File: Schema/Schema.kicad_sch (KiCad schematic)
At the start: 2 parts, among them U1 NodeMCU1.0(ESP-12E)

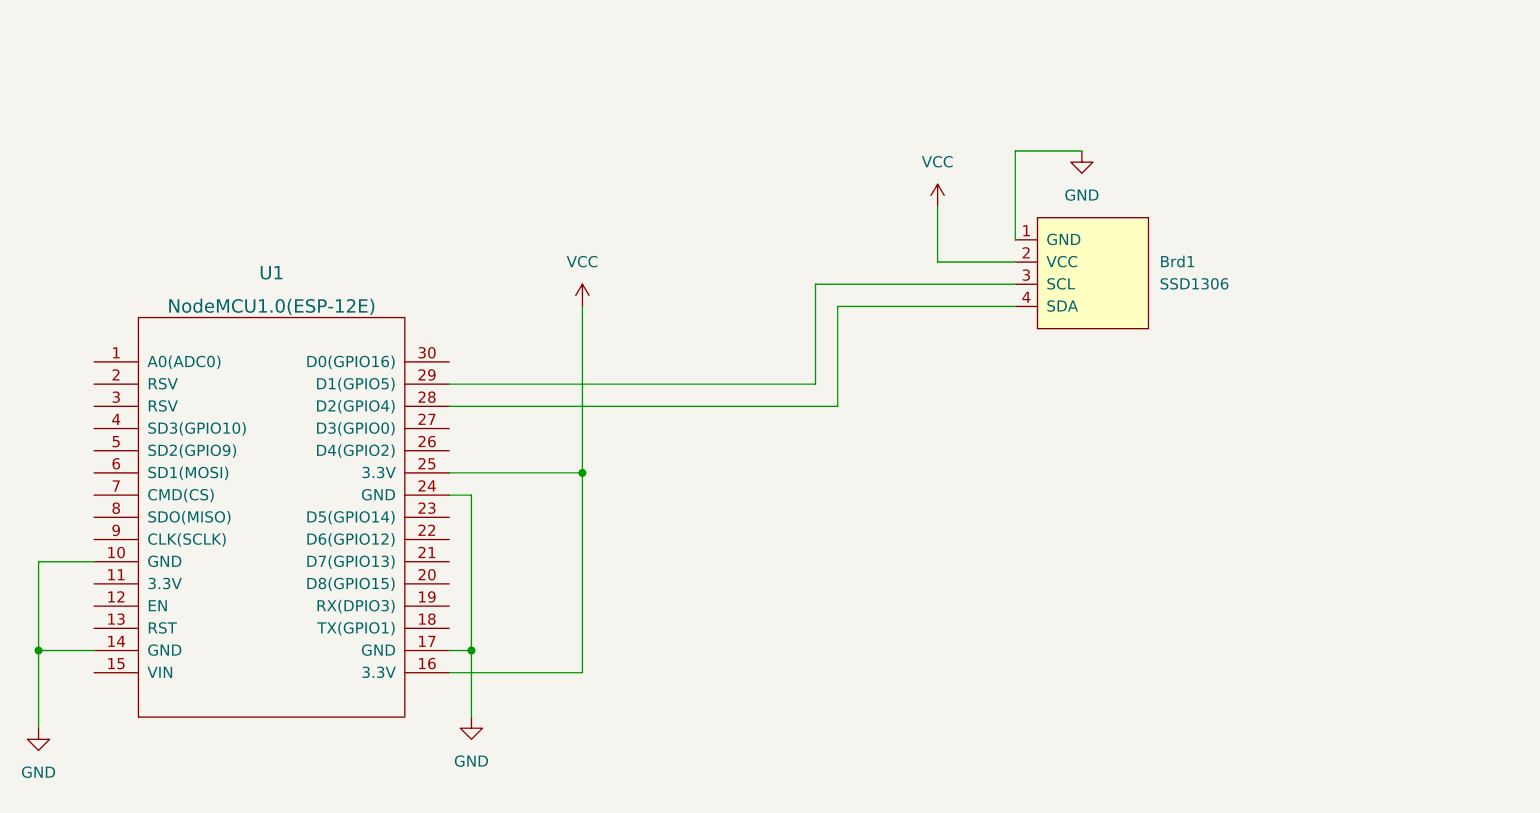
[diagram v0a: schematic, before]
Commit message: Add DHT22
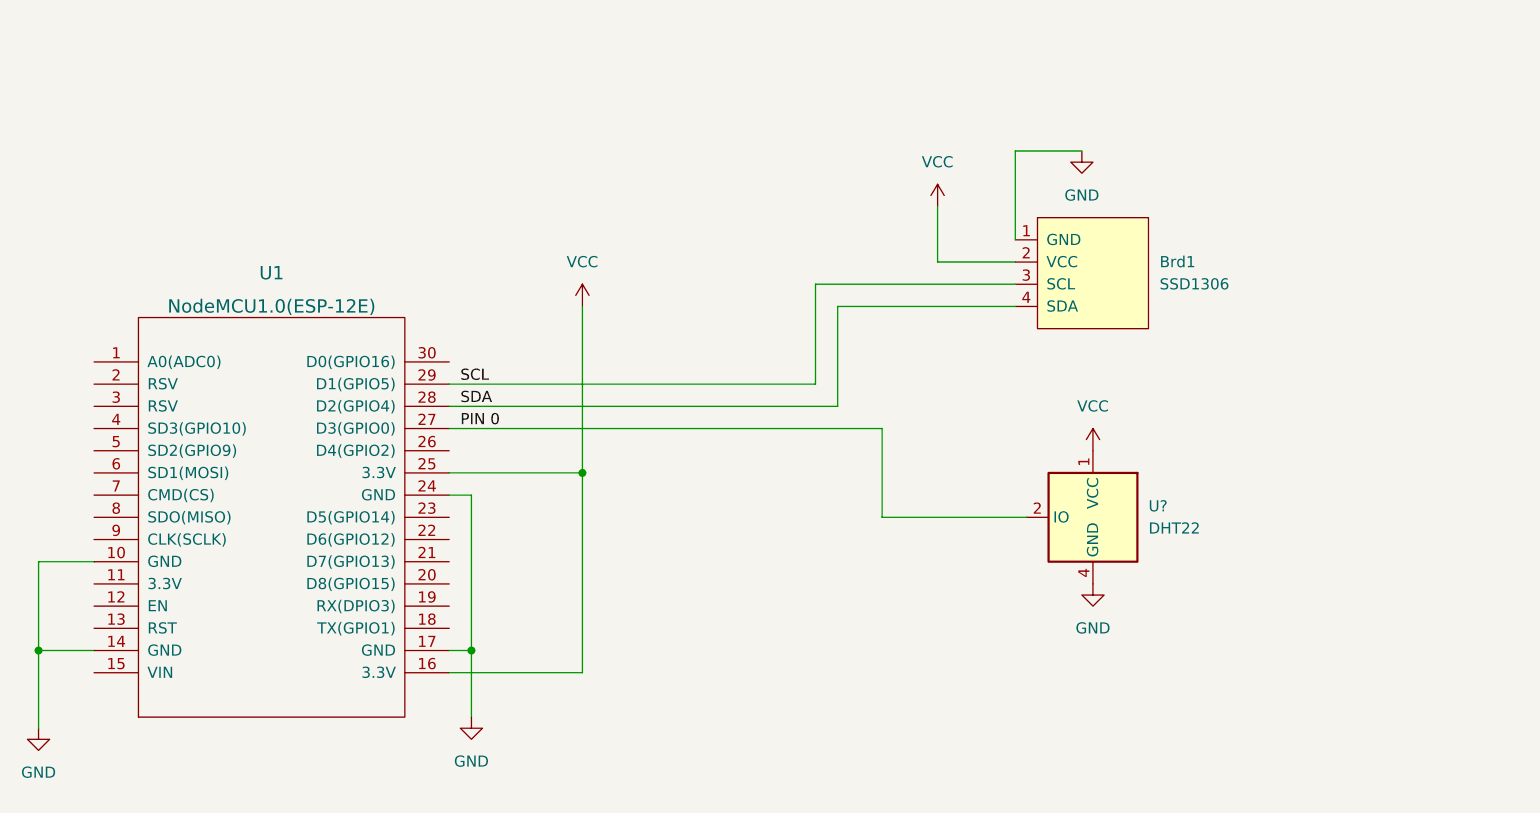
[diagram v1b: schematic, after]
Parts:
- added U?: DHT22, Sensor:Aosong_DHT11_5.5x12.0_P2.54mm, symbol Sensor:DHT11
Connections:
- net GND: now also U?.4 (GND)
- net VCC: now also U?.1 (VCC)
- net SCL: now reaches Brd1.3 (SCL), U1.29 (D1(GPIO5))
- net SDA: now reaches Brd1.4 (SDA), U1.28 (D2(GPIO4))
- net PIN 0: now reaches U1.27 (D3(GPIO0))
- net PIN 0: now also U?.2 (IO)
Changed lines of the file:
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@@
   (junction (at 147.32 90.17) (diameter 0) (color 0 0 0 0)
   )
+  (wire (pts (xy 194.31 64.77) (xy 144.78 64.77))
+    (stroke (width 0) (type default) (color 0 0 0 0))
+  )
+  (wire (pts (xy 194.31 74.93) (xy 194.31 64.77))
+    (stroke (width 0) (type default) (color 0 0 0 0))
+  )
   (wire (pts (xy 147.32 90.17) (xy 147.32 97.79))
     (stroke (width 0) (type default) (color 0 0 0 0))
@@
     (stroke (width 0) (type default) (color 0 0 0 0))
   )
+  (wire (pts (xy 210.82 74.93) (xy 194.31 74.93))
+    (stroke (width 0) (type default) (color 0 0 0 0))
+  )
   (wire (pts (xy 160.02 92.71) (xy 160.02 69.85))
     (stroke (width 0) (type default) (color 0 0 0 0))
@@
   (wire (pts (xy 200.66 39.37) (xy 200.66 45.72))
     (stroke (width 0) (type default) (color 0 0 0 0))
+  )
+  (label "PIN 0" (at 146.05 64.77 0)
+    (effects (font (size 1.27 1.27)) (justify left bottom))
+  )
+  (label "SCL" (at 146.05 59.69 0)
+    (effects (font (size 1.27 1.27)) (justify left bottom))
+  )
+  (label "SDA" (at 146.05 62.23 0)
+    (effects (font (size 1.27 1.27)) (justify left bottom))
   )
   (symbol (lib_id "power:VCC") (at 200.66 39.37 0) (unit 1)
@@
     )
     (property "Datasheet" "" (id 3) (at 147.32 97.79 0)
+      (effects (font (size 1.27 1.27)) hide)
+    )
+    (pin "1")
+  )
+  (symbol (lib_id "power:VCC") (at 218.44 67.31 0) (unit 1)
+    (in_bom yes) (on_board yes) (fields_autoplaced)
+    (property "Reference" "#PWR?" (id 0) (at 218.44 71.12 0)
+      (effects (font (size 1.27 1.27)) hide)
+    )
+    (property "Value" "VCC" (id 1) (at 218.44 62.23 0))
+    (property "Footprint" "" (id 2) (at 218.44 67.31 0)
+      (effects (font (size 1.27 1.27)) hide)
+    )
+    (property "Datasheet" "" (id 3) (at 218.44 67.31 0)
       (effects (font (size 1.27 1.27)) hide)
     )
@@
     )
     (property "Datasheet" "" (id 3) (at 160.02 50.8 0)
+      (effects (font (size 1.27 1.27)) hide)
+    )
+    (pin "1")
+  )
+  (symbol (lib_id "power:GND") (at 218.44 82.55 0) (unit 1)
+    (in_bom yes) (on_board yes) (fields_autoplaced)
+    (property "Reference" "#PWR?" (id 0) (at 218.44 88.9 0)
+      (effects (font (size 1.27 1.27)) hide)
+    )
+    (property "Value" "GND" (id 1) (at 218.44 87.63 0))
+    (property "Footprint" "" (id 2) (at 218.44 82.55 0)
+      (effects (font (size 1.27 1.27)) hide)
+    )
+    (property "Datasheet" "" (id 3) (at 218.44 82.55 0)
       (effects (font (size 1.27 1.27)) hide)
     )
@@
     (pin "9")
   )
+  (symbol (lib_id "Sensor:DHT11") (at 218.44 74.93 0) (mirror y) (unit 1)
+    (in_bom yes) (on_board yes) (fields_autoplaced)
+    (property "Reference" "U?" (id 0) (at 224.79 73.6599 0)
+      (effects (font (size 1.27 1.27)) (justify right))
+    )
+    (property "Value" "DHT22" (id 1) (at 224.79 76.1999 0)
+      (effects (font (size 1.27 1.27)) (justify right))
+    )
+    (property "Footprint" "Sensor:Aosong_DHT11_5.5x12.0_P2.54mm" (id 2) (at 218.44 85.09 0)
+      (effects (font (size 1.27 1.27)) hide)
+    )
+    (property "Datasheet" "http://akizukidenshi.com/download/ds/aosong/DHT11.pdf" (id 3) (at 214.63 68.58 0)
+      (effects (font (size 1.27 1.27)) hide)
+    )
+    (pin "1")
+    (pin "2")
+    (pin "3")
+    (pin "4")
+  )
   (sheet_instances
     (path "/" (page "1"))
@@
       (reference "#PWR05") (unit 1) (value "GND") (footprint "")
     )
+    (path "/499f2d79-bb8d-4d89-9fe8-99f57463159e"
+      (reference "#PWR?") (unit 1) (value "VCC") (footprint "")
+    )
+    (path "/a0466b6d-d396-4959-b837-f499c6288c19"
+      (reference "#PWR?") (unit 1) (value "GND") (footprint "")
+    )
     (path "/4d2f8dec-367b-493f-84d3-db11991c404f"
       (reference "Brd1") (unit 1) (value "SSD1306") (footprint "")
@@
       (reference "U1") (unit 1) (value "NodeMCU1.0(ESP-12E)") (footprint "")
     )
-  )
+    (path "/d224eea1-5f13-4b36-b79c-198fceea3a61"
+      (reference "U?") (unit 1) (value "DHT22") (footprint "Sensor:Aosong_DHT11_5.5x12.0_P2.54mm")
+    )
+  )

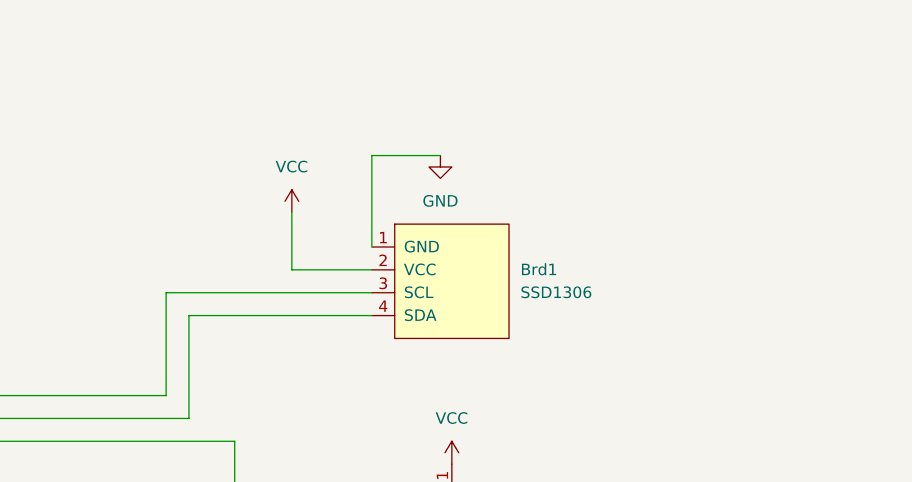
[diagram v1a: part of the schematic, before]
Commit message: add bmp280
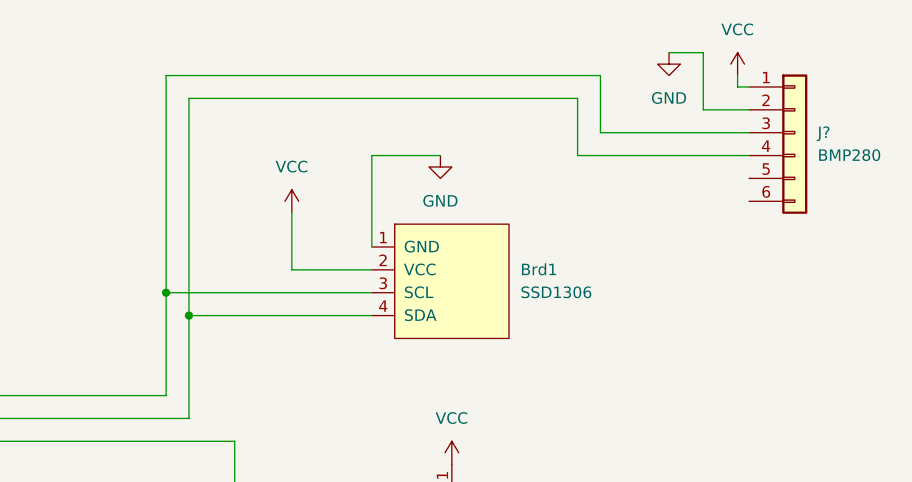
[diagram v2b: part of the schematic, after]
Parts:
- added J?: BMP280, symbol Connector_Generic:Conn_01x06
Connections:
- net GND: now also J?.2 (Pin_2)
- net SCL: now also J?.3 (Pin_3)
- net SDA: now also J?.4 (Pin_4)
- net VCC: now also J?.1 (Pin_1)

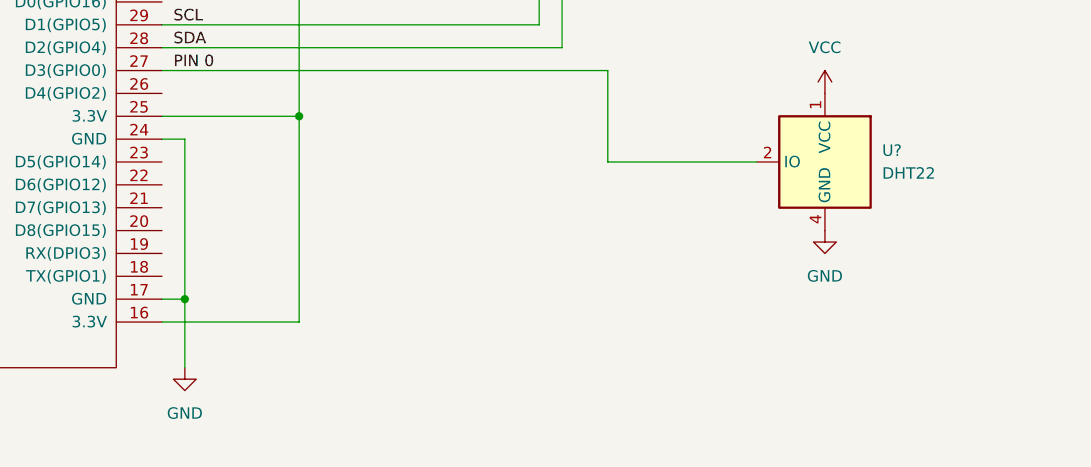
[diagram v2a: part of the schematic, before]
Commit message: Add CO2
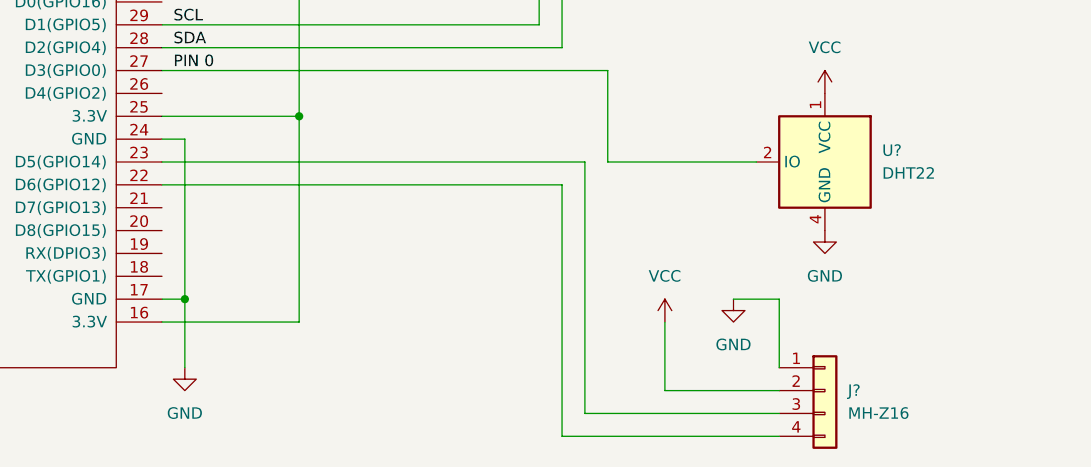
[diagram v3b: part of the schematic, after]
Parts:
- added J?: MH-Z16, symbol Connector_Generic:Conn_01x04
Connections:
- net GND: now also J?.1 (Pin_1)
- net VCC: now also J?.2 (Pin_2)
- net at U1.22 (D6(GPIO12)): now also J?.4 (Pin_4)
- net at U1.23 (D5(GPIO14)): now also J?.3 (Pin_3)
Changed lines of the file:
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@@
+    (stroke (width 0) (type default) (color 0 0 0 0))
+  )
+  (wire (pts (xy 191.77 74.93) (xy 191.77 102.87))
     (stroke (width 0) (type default) (color 0 0 0 0))
   )
@@
     (stroke (width 0) (type default) (color 0 0 0 0))
   )
+  (wire (pts (xy 189.23 105.41) (xy 213.36 105.41))
+    (stroke (width 0) (type default) (color 0 0 0 0))
+  )
   (wire (pts (xy 232.41 33.02) (xy 232.41 26.67))
     (stroke (width 0) (type default) (color 0 0 0 0))
@@
     (stroke (width 0) (type default) (color 0 0 0 0))
   )
+  (wire (pts (xy 213.36 90.17) (xy 208.28 90.17))
+    (stroke (width 0) (type default) (color 0 0 0 0))
+  )
+  (wire (pts (xy 144.78 74.93) (xy 191.77 74.93))
+    (stroke (width 0) (type default) (color 0 0 0 0))
+  )
   (wire (pts (xy 217.17 33.02) (xy 209.55 33.02))
     (stroke (width 0) (type default) (color 0 0 0 0))
@@
     (stroke (width 0) (type default) (color 0 0 0 0))
   )
+  (wire (pts (xy 189.23 105.41) (xy 189.23 77.47))
+    (stroke (width 0) (type default) (color 0 0 0 0))
+  )
   (wire (pts (xy 209.55 50.8) (xy 189.23 50.8))
     (stroke (width 0) (type default) (color 0 0 0 0))
@@
     (stroke (width 0) (type default) (color 0 0 0 0))
   )
+  (wire (pts (xy 200.66 100.33) (xy 200.66 92.71))
+    (stroke (width 0) (type default) (color 0 0 0 0))
+  )
+  (wire (pts (xy 213.36 97.79) (xy 213.36 90.17))
+    (stroke (width 0) (type default) (color 0 0 0 0))
+  )
   (wire (pts (xy 104.14 80.01) (xy 97.79 80.01))
     (stroke (width 0) (type default) (color 0 0 0 0))
@@
     (stroke (width 0) (type default) (color 0 0 0 0))
   )
+  (wire (pts (xy 189.23 77.47) (xy 144.78 77.47))
+    (stroke (width 0) (type default) (color 0 0 0 0))
+  )
   (wire (pts (xy 250.19 25.4) (xy 251.46 25.4))
     (stroke (width 0) (type default) (color 0 0 0 0))
   )
+  (wire (pts (xy 213.36 100.33) (xy 200.66 100.33))
+    (stroke (width 0) (type default) (color 0 0 0 0))
+  )
   (wire (pts (xy 234.95 30.48) (xy 251.46 30.48))
     (stroke (width 0) (type default) (color 0 0 0 0))
@@
   )
   (wire (pts (xy 186.69 24.13) (xy 186.69 48.26))
+    (stroke (width 0) (type default) (color 0 0 0 0))
+  )
+  (wire (pts (xy 191.77 102.87) (xy 213.36 102.87))
     (stroke (width 0) (type default) (color 0 0 0 0))
   )
@@
     (pin "1")
   )
+  (symbol (lib_id "power:VCC") (at 200.66 92.71 0) (unit 1)
+    (in_bom yes) (on_board yes) (fields_autoplaced)
+    (property "Reference" "#PWR?" (id 0) (at 200.66 96.52 0)
+      (effects (font (size 1.27 1.27)) hide)
+    )
+    (property "Value" "VCC" (id 1) (at 200.66 87.63 0))
+    (property "Footprint" "" (id 2) (at 200.66 92.71 0)
+      (effects (font (size 1.27 1.27)) hide)
+    )
+    (property "Datasheet" "" (id 3) (at 200.66 92.71 0)
+      (effects (font (size 1.27 1.27)) hide)
+    )
+    (pin "1")
+  )
   (symbol (lib_id "power:VCC") (at 218.44 67.31 0) (unit 1)
     (in_bom yes) (on_board yes) (fields_autoplaced)
@@
     )
     (property "Datasheet" "" (id 3) (at 212.09 46.99 0)
+      (effects (font (size 1.27 1.27)) hide)
+    )
+    (pin "1")
+    (pin "2")
+    (pin "3")
+    (pin "4")
+  )
+  (symbol (lib_id "power:GND") (at 208.28 90.17 0) (unit 1)
+    (in_bom yes) (on_board yes) (fields_autoplaced)
+    (property "Reference" "#PWR?" (id 0) (at 208.28 96.52 0)
+      (effects (font (size 1.27 1.27)) hide)
+    )
+    (property "Value" "GND" (id 1) (at 208.28 95.25 0))
+    (property "Footprint" "" (id 2) (at 208.28 90.17 0)
+      (effects (font (size 1.27 1.27)) hide)
+    )
+    (property "Datasheet" "" (id 3) (at 208.28 90.17 0)
+      (effects (font (size 1.27 1.27)) hide)
+    )
+    (pin "1")
+  )
+  (symbol (lib_id "Connector_Generic:Conn_01x04") (at 218.44 100.33 0) (unit 1)
+    (in_bom yes) (on_board yes) (fields_autoplaced)
+    (property "Reference" "J?" (id 0) (at 220.98 100.3299 0)
+      (effects (font (size 1.27 1.27)) (justify left))
+    )
+    (property "Value" "MH-Z16" (id 1) (at 220.98 102.8699 0)
+      (effects (font (size 1.27 1.27)) (justify left))
+    )
+    (property "Footprint" "" (id 2) (at 218.44 100.33 0)
+      (effects (font (size 1.27 1.27)) hide)
+    )
+    (property "Datasheet" "~" (id 3) (at 218.44 100.33 0)
       (effects (font (size 1.27 1.27)) hide)
     )
@@
       (reference "#PWR05") (unit 1) (value "GND") (footprint "")
     )
+    (path "/3d1d5007-d4ae-4cb9-a031-ed58dcd72d63"
+      (reference "#PWR?") (unit 1) (value "VCC") (footprint "")
+    )
     (path "/499f2d79-bb8d-4d89-9fe8-99f57463159e"
       (reference "#PWR?") (unit 1) (value "VCC") (footprint "")
     )
+    (path "/60731262-1e08-498a-8b00-4981bca6df3d"
+      (reference "#PWR?") (unit 1) (value "GND") (footprint "")
+    )
     (path "/9920fdcf-6e8c-4a5a-a9bd-d9d145a50358"
       (reference "#PWR?") (unit 1) (value "GND") (footprint "")
@@
       (reference "J?") (unit 1) (value "BMP280") (footprint "")
     )
+    (path "/80e53fdd-e478-46f9-83d2-a754d84a6530"
+      (reference "J?") (unit 1) (value "MH-Z16") (footprint "")
+    )
     (path "/cf43512a-d7c1-4975-b822-ada7cfdefde7"
